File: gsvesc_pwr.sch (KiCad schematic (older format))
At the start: 57 parts, among them J10 PHASE_A, J12 NTC, U7 M74VHC1GT66DTT1G, U8 M74VHC1GT66DTT1G, U9 M74VHC1GT66DTT1G

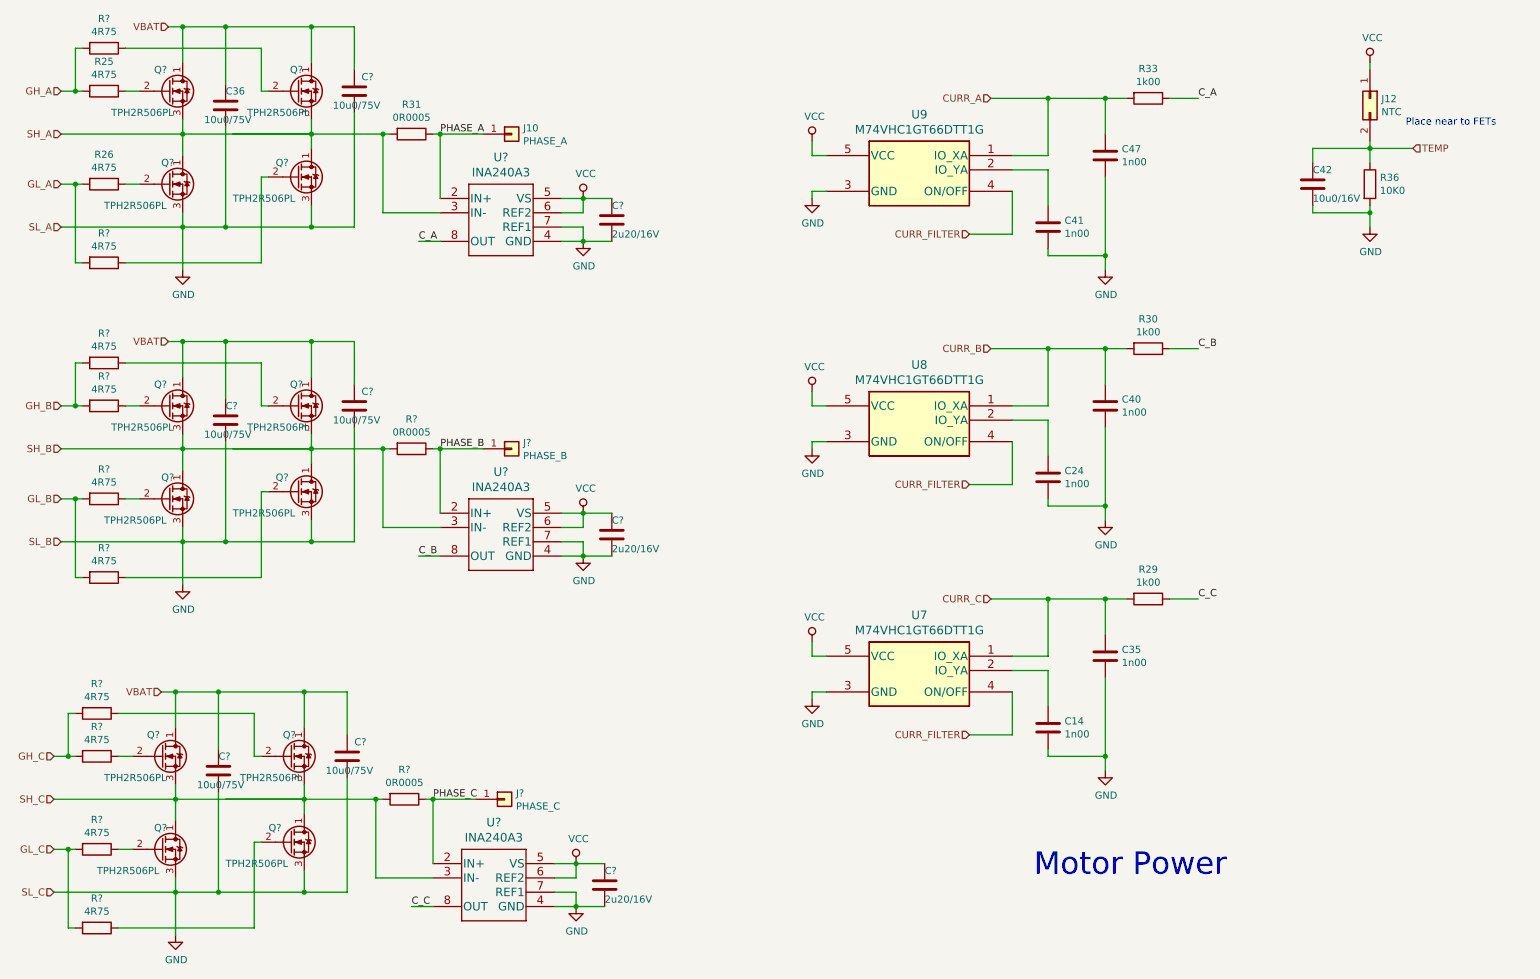
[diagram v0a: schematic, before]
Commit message: First Version V3 - Change FET to TPH2R506PL - 1oz copper on all layer - switch analog amp to INA240 - remove Elkos - add more ceramic c - separate current measurement tracks from gate driver tracks - vbat now 36V
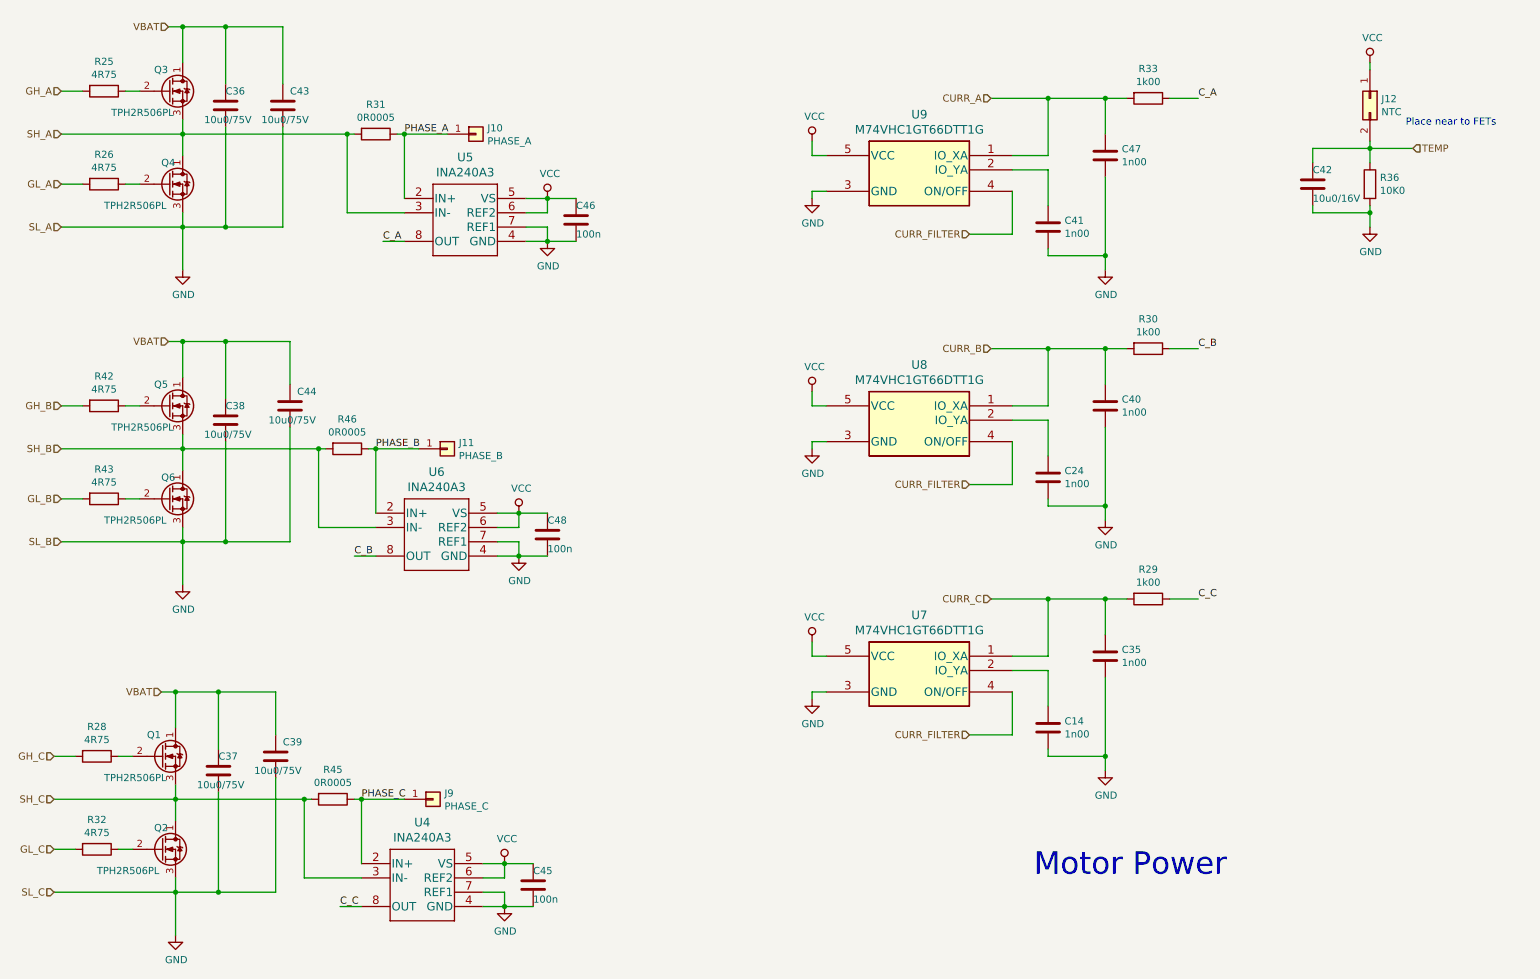
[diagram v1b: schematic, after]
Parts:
- removed Q? (x6): TPH2R506PL, symbol gsvesc:TPH2R506PL
- removed R? (x6): 4R75, Resistor_SMD:R_0805_2012Metric, symbol Device:R
- C45, C46, C48: renamed from C?; value 2u20/16V -> 100n
- Q1, Q2, Q3, Q4, Q5, Q6: renamed from Q?; footprint (none) -> gsvesc:TRANS_TPHR8504PL-3PIN
- U4, U5, U6: renamed from U?; footprint PW0008A_N -> gsvesc:INA240A1QPWRQ1
- gave numbers to parts that had none: 13
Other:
- moved on the sheet: C39, C43, C44, C45, C46, C48, J10, J11, J9, R31, R45, R46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

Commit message: Version 3 update - JST as SMD part - move FET tracks
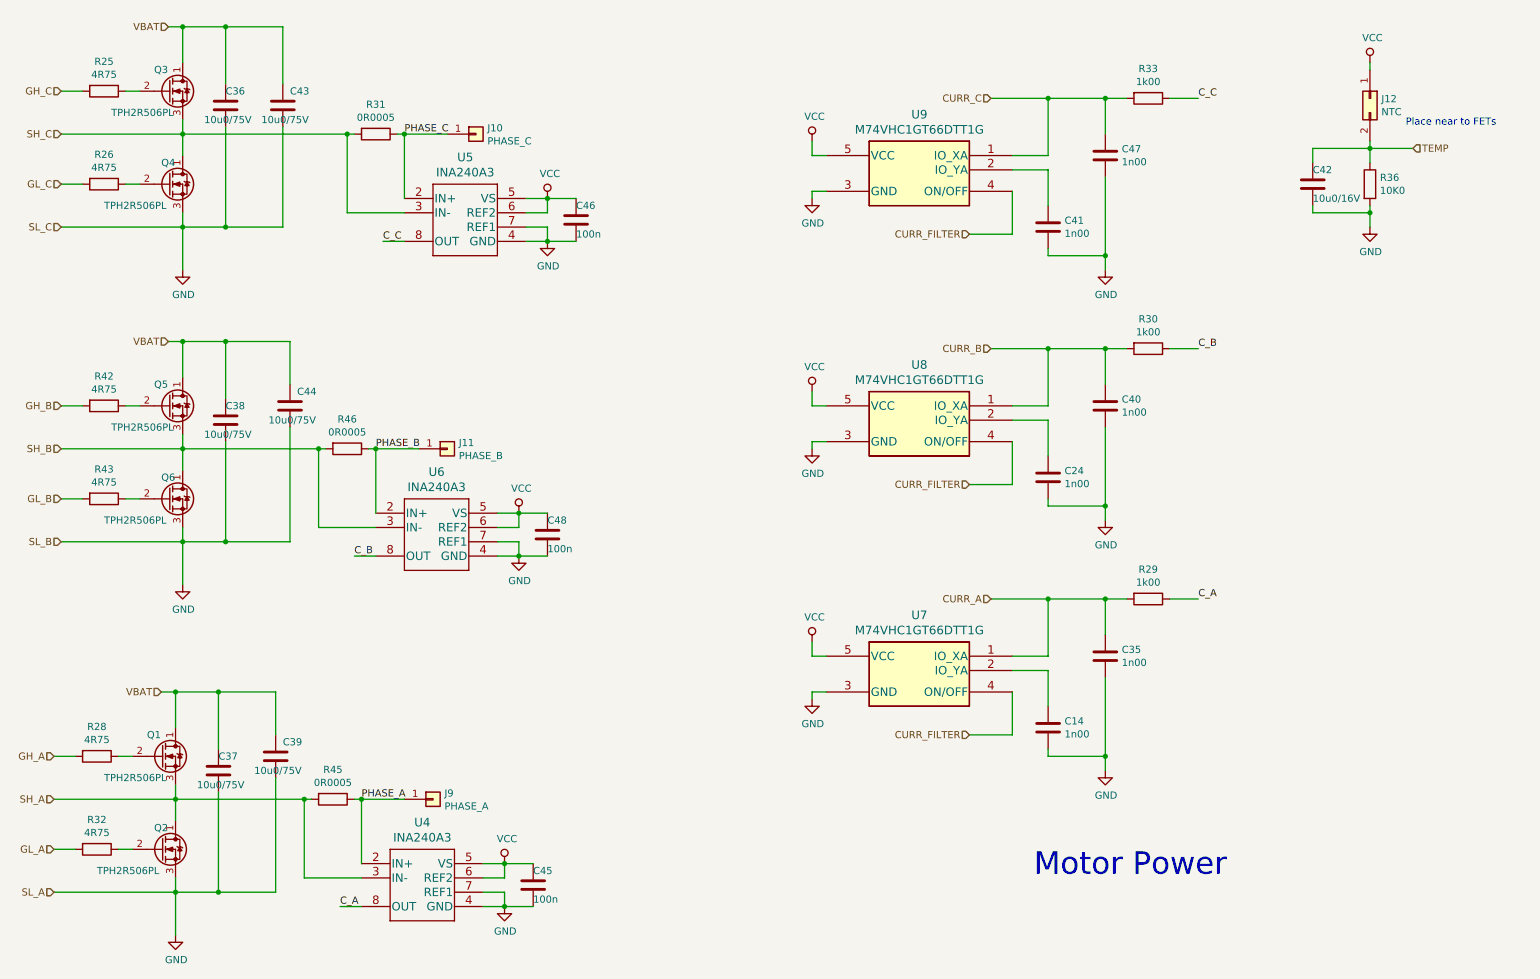
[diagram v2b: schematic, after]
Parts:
- J10: value PHASE_A -> PHASE_C
- J9: value PHASE_C -> PHASE_A
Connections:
- net CURR_A: now also C35.1, R29.2, U7.1 (IO_XA); no longer C47.1, R33.2, U9.1 (IO_XA)
- net CURR_C: now also C47.1, R33.2, U9.1 (IO_XA); no longer C35.1, R29.2, U7.1 (IO_XA)
- net C_A: now also R29.1, U4.8 (OUT); no longer R33.1, U5.8 (OUT)
- net C_C: now also R33.1, U5.8 (OUT); no longer R29.1, U4.8 (OUT)
- net GH_A: now also R28.2; no longer R25.2
- net GH_C: now also R25.2; no longer R28.2
- net GL_A: now also R32.2; no longer R26.2
- net GL_C: now also R26.2; no longer R32.2
- net PHASE_A: now also J9.1 (Pin_1), R45.1, U4.2 (IN+); no longer J10.1 (Pin_1), R31.1, U5.2 (IN+)
- net PHASE_C: now also J10.1 (Pin_1), R31.1, U5.2 (IN+); no longer J9.1 (Pin_1), R45.1, U4.2 (IN+)
- net SH_A: now also Q1.3 (S), Q2.1 (D), R45.2, U4.3 (IN-); no longer Q3.3 (S), Q4.1 (D), R31.2, U5.3 (IN-)
- net SH_C: now also Q3.3 (S), Q4.1 (D), R31.2, U5.3 (IN-); no longer Q1.3 (S), Q2.1 (D), R45.2, U4.3 (IN-)
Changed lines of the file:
@@
 P 3800 1600
 F 0 "J10" H 3880 1642 50  0000 L CNN
-F 1 "PHASE_A" H 3880 1551 50  0000 L CNN
+F 1 "PHASE_C" H 3880 1551 50  0000 L CNN
 F 2 "gsvesc:TestPoint_Pad_5.0x5.0mm" H 3800 1600 50  0001 C CNN
 F 3 "~" H 3800 1600 50  0001 C CNN
@@
 	3300 1600 3600 1600
 Text HLabel 900  1300 0    50   Input ~ 0
-GH_A
+GH_C
 Text HLabel 900  1950 0    50   Input ~ 0
-GL_A
+GL_C
 Wire Wire Line
 	900  2250 1750 2250
 Text HLabel 900  1600 0    50   Input ~ 0
-SH_A
+SH_C
 Text HLabel 900  2250 0    50   Input ~ 0
-SL_A
+SL_C
 $Comp
 L Device:R R29
@@
 $EndComp
 Text HLabel 7400 4850 0    50   Input ~ 0
-CURR_C
+CURR_A
 $Comp
 L Device:R R36
@@
 Connection ~ 3300 1600
 Text Label 3300 1600 0    50   ~ 0
-PHASE_A
+PHASE_C
 $Comp
 L gsvesc:M74VHC1GT66DTT1G U7
@@
 	8650 1350 8850 1350
 Text Label 8850 1350 0    50   ~ 0
-C_A
+C_C
 Wire Wire Line
 	8200 1900 8200 2450
@@
 $EndComp
 Text HLabel 7400 1350 0    50   Input ~ 0
-CURR_A
+CURR_C
 $Comp
 L gsvesc:M74VHC1GT66DTT1G U9
@@
 	3300 2350 3150 2350
 Text Label 3150 2350 0    50   ~ 0
-C_A
+C_C
 Wire Wire Line
 	1650 850  1750 850
@@
 P 3500 6250
 F 0 "J9" H 3580 6292 50  0000 L CNN
-F 1 "PHASE_C" H 3580 6201 50  0000 L CNN
+F 1 "PHASE_A" H 3580 6201 50  0000 L CNN
 F 2 "gsvesc:TestPoint_Pad_5.0x5.0mm" H 3500 6250 50  0001 C CNN
 F 3 "~" H 3500 6250 50  0001 C CNN
@@
 	3000 6250 3300 6250
 Text HLabel 850  5950 0    50   Input ~ 0
-GH_C
+GH_A
 Text HLabel 850  6600 0    50   Input ~ 0
-GL_C
+GL_A
 Wire Wire Line
 	850  6900 1700 6900
 Text HLabel 850  6250 0    50   Input ~ 0
-SH_C
+SH_A
 Text HLabel 850  6900 0    50   Input ~ 0
-SL_C
+SL_A
 Wire Wire Line
 	850  6250 1700 6250
@@
 Connection ~ 3000 6250
 Text Label 3000 6250 0    50   ~ 0
-PHASE_C
+PHASE_A
 $Comp
 L gsvesc:TPH2R506PL Q1
@@
 	3000 7000 2850 7000
 Text Label 2850 7000 0    50   ~ 0
-C_C
+C_A
 Wire Wire Line
 	1600 5500 1700 5500
@@
 	1700 6250 2600 6250
 Text Label 8850 4850 0    50   ~ 0
-C_C
+C_A
 Wire Wire Line
 	900  1300 1050 1300

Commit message: V4 first version
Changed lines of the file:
@@
 $Descr A4 11693 8268
 encoding utf-8
-Sheet 4 5
+Sheet 5 5
 Title "GSESC - DC Motor Controler"
 Date "2018-11-11"
-Rev "3.0"
+Rev "4.0"
 Comp ""
 Comment1 ""
@@
 Comment4 ""
 $EndDescr
-Text Notes 7700 6800 0    157  ~ 0
+Text Notes 7100 6950 0    157  ~ 0
 Motor Power
 $Comp
@@
 Wire Wire Line
 	1750 1100 1750 850
-Text HLabel 1650 850  0    50   Input ~ 0
-VBAT
 Wire Wire Line
 	1350 1300 1450 1300
@@
 Text HLabel 900  1950 0    50   Input ~ 0
 GL_C
-Wire Wire Line
-	900  2250 1750 2250
 Text HLabel 900  1600 0    50   Input ~ 0
 SH_C
-Text HLabel 900  2250 0    50   Input ~ 0
-SL_C
 $Comp
 L Device:R R29
@@
 Wire Wire Line
 	1750 3300 1750 3050
-Text HLabel 1650 3050 0    50   Input ~ 0
-VBAT
 Wire Wire Line
 	1350 3500 1450 3500
@@
 Text HLabel 900  3800 0    50   Input ~ 0
 SH_B
-Text HLabel 900  4450 0    50   Input ~ 0
-SL_B
 $Comp
 L Device:R R46
@@
 Wire Wire Line
 	1700 5750 1700 5500
-Text HLabel 1600 5500 0    50   Input ~ 0
-VBAT
 Wire Wire Line
 	1300 5950 1400 5950
@@
 Text HLabel 850  6600 0    50   Input ~ 0
 GL_A
-Wire Wire Line
-	850  6900 1700 6900
 Text HLabel 850  6250 0    50   Input ~ 0
 SH_A
-Text HLabel 850  6900 0    50   Input ~ 0
-SL_A
 Wire Wire Line
 	850  6250 1700 6250
@@
 	900  3800 1750 3800
 Wire Wire Line
-	900  4450 1750 4450
-Wire Wire Line
 	2050 4450 2500 4450
 Connection ~ 2050 4450
@@
 	2000 5500 2400 5500
 Connection ~ 2000 5500
+Text GLabel 1650 850  0    50   Input ~ 0
+VBAT
+Text GLabel 1650 3050 0    50   Input ~ 0
+VBAT
+Text GLabel 1600 5500 0    50   Input ~ 0
+VBAT
 $EndSCHEMATC

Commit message: Power Supply geändert
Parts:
- C42: value 10u0/16V -> 10u0/25V
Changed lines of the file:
@@
 P 9650 1950
 F 0 "C42" H 9650 2050 50  0000 L CNN
-F 1 "10u0/16V" H 9650 1850 50  0000 L CNN
+F 1 "10u0/25V" H 9650 1850 50  0000 L CNN
 F 2 "Capacitor_SMD:C_0805_2012Metric" H 9688 1800 50  0001 C CNN
 F 3 "~" H 9650 1950 50  0001 C CNN

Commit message: Powersupply geändert
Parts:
- C14, C24, C41: value 1n00 -> 10n0
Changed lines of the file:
@@
 P 7800 5750
 F 0 "C14" H 7915 5796 50  0000 L CNN
-F 1 "1n00" H 7915 5705 50  0000 L CNN
+F 1 "10n0" H 7915 5705 50  0000 L CNN
 F 2 "Capacitor_SMD:C_0805_2012Metric" H 7838 5600 50  0001 C CNN
 F 3 "~" H 7800 5750 50  0001 C CNN
@@
 P 7800 4000
 F 0 "C24" H 7915 4046 50  0000 L CNN
-F 1 "1n00" H 7915 3955 50  0000 L CNN
+F 1 "10n0" H 7915 3955 50  0000 L CNN
 F 2 "Capacitor_SMD:C_0805_2012Metric" H 7838 3850 50  0001 C CNN
 F 3 "~" H 7800 4000 50  0001 C CNN
@@
 P 7800 2250
 F 0 "C41" H 7915 2296 50  0000 L CNN
-F 1 "1n00" H 7915 2205 50  0000 L CNN
+F 1 "10n0" H 7915 2205 50  0000 L CNN
 F 2 "Capacitor_SMD:C_0805_2012Metric" H 7838 2100 50  0001 C CNN
 F 3 "~" H 7800 2250 50  0001 C CNN

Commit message: V4 pre
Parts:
- J12: footprint Connector_PinHeader_2.54mm:PinHeader_2x01_P2.54mm_Vertical -> gsvesc:2pad_smd_testpin
- Q1, Q2, Q4, Q5, Q6: LCSC (none) -> C146377; Partnumber (none) -> TPH2R608NH
- Q3: symbol gsvesc:TPH2R506PL -> gsvesc:TPH2R608NH; LCSC (none) -> C146377; Partnumber (none) -> TPH2R608NH
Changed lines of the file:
@@
 F 0 "J12" V 10054 1430 50  0000 L CNN
 F 1 "NTC" V 10145 1430 50  0000 L CNN
-F 2 "Connector_PinHeader_2.54mm:PinHeader_2x01_P2.54mm_Vertical" H 10050 1350 50  0001 C CNN
+F 2 "gsvesc:2pad_smd_testpin" H 10050 1350 50  0001 C CNN
 F 3 "~" H 10050 1350 50  0001 C CNN
 	1    10050 1350
@@
 	6150 2000 6150 2050
 $Comp
-L gsvesc:TPH2R506PL Q3
+L gsvesc:TPH2R608NH Q3
 U 1 1 5E3D365F
 P 1650 1300
@@
 F 2 "gsvesc:TRANS_TPHR8504PL-3PIN" H 1650 1300 50  0001 C CIN
 F 3 "" H 1650 1300 50  0001 L CNN
+F 4 "C146377" H 0   0   50  0001 C CNN "LCSC"
+F 5 "TPH2R608NH" H 0   0   50  0001 C CNN "Partnumber"
 	1    1650 1300
 	1    0    0    -1
@@
 F 2 "gsvesc:TRANS_TPHR8504PL-3PIN" H 1650 1950 50  0001 C CIN
 F 3 "" H 1650 1950 50  0001 L CNN
+F 4 "C146377" H 0   0   50  0001 C CNN "LCSC"
+F 5 "TPH2R608NH" H 0   0   50  0001 C CNN "Partnumber"
 	1    1650 1950
 	1    0    0    -1
@@
 F 2 "gsvesc:TRANS_TPHR8504PL-3PIN" H 1650 3500 50  0001 C CIN
 F 3 "" H 1650 3500 50  0001 L CNN
+F 4 "C146377" H 0   0   50  0001 C CNN "LCSC"
+F 5 "TPH2R608NH" H 0   0   50  0001 C CNN "Partnumber"
 	1    1650 3500
 	1    0    0    -1
@@
 F 2 "gsvesc:TRANS_TPHR8504PL-3PIN" H 1650 4150 50  0001 C CIN
 F 3 "" H 1650 4150 50  0001 L CNN
+F 4 "C146377" H 0   0   50  0001 C CNN "LCSC"
+F 5 "TPH2R608NH" H 0   0   50  0001 C CNN "Partnumber"
 	1    1650 4150
 	1    0    0    -1
@@
 F 2 "gsvesc:TRANS_TPHR8504PL-3PIN" H 1600 5950 50  0001 C CIN
 F 3 "" H 1600 5950 50  0001 L CNN
+F 4 "C146377" H 0   0   50  0001 C CNN "LCSC"
+F 5 "TPH2R608NH" H 0   0   50  0001 C CNN "Partnumber"
 	1    1600 5950
 	1    0    0    -1
@@
 F 2 "gsvesc:TRANS_TPHR8504PL-3PIN" H 1600 6600 50  0001 C CIN
 F 3 "" H 1600 6600 50  0001 L CNN
+F 4 "C146377" H 0   0   50  0001 C CNN "LCSC"
+F 5 "TPH2R608NH" H 0   0   50  0001 C CNN "Partnumber"
 	1    1600 6600
 	1    0    0    -1

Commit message: V4 alpha
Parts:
- Q1, Q2, Q3, Q4, Q5, Q6: value TPH2R506PL -> TPH2R608NH,L1Q
- R31, R45, R46: value 0R0005 -> 0R001
- R36: value 10K0 -> 10k0
- U4, U5, U6: value INA240A3 -> INA240A2
- U7, U8, U9: value M74VHC1GT66DTT1G -> SN74LVC1G66DBVR
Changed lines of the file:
@@
 P 10050 1950
 F 0 "R36" H 10120 1996 50  0000 L CNN
-F 1 "10K0" H 10120 1905 50  0000 L CNN
+F 1 "10k0" H 10120 1905 50  0000 L CNN
 F 2 "Resistor_SMD:R_0805_2012Metric" V 9980 1950 50  0001 C CNN
 F 3 "~" H 10050 1950 50  0001 C CNN
@@
 P 3100 1600
 F 0 "R31" V 2893 1600 50  0000 C CNN
-F 1 "0R0005" V 2984 1600 50  0000 C CNN
+F 1 "0R001" V 2984 1600 50  0000 C CNN
 F 2 "Resistor_SMD:R_2512_6332Metric" V 3030 1600 50  0001 C CNN
 F 3 "~" H 3100 1600 50  0001 C CNN
@@
 P 6250 5450
 F 0 "U7" H 6900 5937 60  0000 C CNN
-F 1 "M74VHC1GT66DTT1G" H 6900 5831 60  0000 C CNN
+F 1 "SN74LVC1G66DBVR" H 6900 5831 60  0000 C CNN
 F 2 "gsvesc:M74VHC1GT66DTT1G" H 6750 5250 60  0001 C CNN
 F 3 "" H 6250 5450 60  0000 C CNN
@@
 P 6250 3700
 F 0 "U8" H 6900 4187 60  0000 C CNN
-F 1 "M74VHC1GT66DTT1G" H 6900 4081 60  0000 C CNN
+F 1 "SN74LVC1G66DBVR" H 6900 4081 60  0000 C CNN
 F 2 "gsvesc:M74VHC1GT66DTT1G" H 6750 3500 60  0001 C CNN
 F 3 "" H 6250 3700 60  0000 C CNN
@@
 P 6250 1950
 F 0 "U9" H 6900 2437 60  0000 C CNN
-F 1 "M74VHC1GT66DTT1G" H 6900 2331 60  0000 C CNN
+F 1 "SN74LVC1G66DBVR" H 6900 2331 60  0000 C CNN
 F 2 "gsvesc:M74VHC1GT66DTT1G" H 6750 1750 60  0001 C CNN
 F 3 "" H 6250 1950 60  0000 C CNN
@@
 P 1650 1300
 F 0 "Q3" H 1550 1450 50  0000 L CNN
-F 1 "TPH2R506PL" H 1250 1150 50  0000 L CNN
+F 1 "TPH2R608NH,L1Q" H 1250 1150 50  0000 L CNN
 F 2 "gsvesc:TRANS_TPHR8504PL-3PIN" H 1650 1300 50  0001 C CIN
 F 3 "" H 1650 1300 50  0001 L CNN
@@
 P 1650 1950
 F 0 "Q4" H 1600 2100 50  0000 L CNN
-F 1 "TPH2R506PL" H 1200 1800 50  0000 L CNN
+F 1 "TPH2R608NH,L1Q" H 1200 1800 50  0000 L CNN
 F 2 "gsvesc:TRANS_TPHR8504PL-3PIN" H 1650 1950 50  0001 C CIN
 F 3 "" H 1650 1950 50  0001 L CNN
@@
 P 4000 2450
 F 0 "U5" H 3725 3138 60  0000 C CNN
-F 1 "INA240A3" H 3725 3032 60  0000 C CNN
+F 1 "INA240A2" H 3725 3032 60  0000 C CNN
 F 2 "gsvesc:INA240A1QPWRQ1" H 3750 2400 60  0001 C CNN
 F 3 "" H 4000 2450 60  0000 C CNN
@@
 P 2900 3800
 F 0 "R46" V 2693 3800 50  0000 C CNN
-F 1 "0R0005" V 2784 3800 50  0000 C CNN
+F 1 "0R001" V 2784 3800 50  0000 C CNN
 F 2 "Resistor_SMD:R_2512_6332Metric" V 2830 3800 50  0001 C CNN
 F 3 "~" H 2900 3800 50  0001 C CNN
@@
 P 1650 3500
 F 0 "Q5" H 1550 3650 50  0000 L CNN
-F 1 "TPH2R506PL" H 1250 3350 50  0000 L CNN
+F 1 "TPH2R608NH,L1Q" H 1250 3350 50  0000 L CNN
 F 2 "gsvesc:TRANS_TPHR8504PL-3PIN" H 1650 3500 50  0001 C CIN
 F 3 "" H 1650 3500 50  0001 L CNN
@@
 P 1650 4150
 F 0 "Q6" H 1600 4300 50  0000 L CNN
-F 1 "TPH2R506PL" H 1200 4000 50  0000 L CNN
+F 1 "TPH2R608NH,L1Q" H 1200 4000 50  0000 L CNN
 F 2 "gsvesc:TRANS_TPHR8504PL-3PIN" H 1650 4150 50  0001 C CIN
 F 3 "" H 1650 4150 50  0001 L CNN
@@
 P 3800 4650
 F 0 "U6" H 3525 5338 60  0000 C CNN
-F 1 "INA240A3" H 3525 5232 60  0000 C CNN
+F 1 "INA240A2" H 3525 5232 60  0000 C CNN
 F 2 "gsvesc:INA240A1QPWRQ1" H 3550 4600 60  0001 C CNN
 F 3 "" H 3800 4650 60  0000 C CNN
@@
 P 2800 6250
 F 0 "R45" V 2593 6250 50  0000 C CNN
-F 1 "0R0005" V 2684 6250 50  0000 C CNN
+F 1 "0R001" V 2684 6250 50  0000 C CNN
 F 2 "Resistor_SMD:R_2512_6332Metric" V 2730 6250 50  0001 C CNN
 F 3 "~" H 2800 6250 50  0001 C CNN
@@
 P 1600 5950
 F 0 "Q1" H 1500 6100 50  0000 L CNN
-F 1 "TPH2R506PL" H 1200 5800 50  0000 L CNN
+F 1 "TPH2R608NH,L1Q" H 1200 5800 50  0000 L CNN
 F 2 "gsvesc:TRANS_TPHR8504PL-3PIN" H 1600 5950 50  0001 C CIN
 F 3 "" H 1600 5950 50  0001 L CNN
@@
 P 1600 6600
 F 0 "Q2" H 1550 6750 50  0000 L CNN
-F 1 "TPH2R506PL" H 1150 6450 50  0000 L CNN
+F 1 "TPH2R608NH,L1Q" H 1150 6450 50  0000 L CNN
 F 2 "gsvesc:TRANS_TPHR8504PL-3PIN" H 1600 6600 50  0001 C CIN
 F 3 "" H 1600 6600 50  0001 L CNN
@@
 P 3700 7100
 F 0 "U4" H 3425 7788 60  0000 C CNN
-F 1 "INA240A3" H 3425 7682 60  0000 C CNN
+F 1 "INA240A2" H 3425 7682 60  0000 C CNN
 F 2 "gsvesc:INA240A1QPWRQ1" H 3450 7050 60  0001 C CNN
 F 3 "" H 3700 7100 60  0000 C CNN

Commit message: temp
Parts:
- added C50, C51, C52: 10u0/75V, Capacitor_SMD:C_1210_3225Metric, symbol Device:C
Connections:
- net GND: now also C50.2, C51.2, C52.2
- net VBAT: now also C50.1, C51.1, C52.1
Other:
- moved on the sheet: C45, C46, C48, J10, J11, J9, R31, R45, R46, U4, U5, U6
